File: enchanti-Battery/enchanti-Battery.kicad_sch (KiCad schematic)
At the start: 19 parts, among them U1 BQ25185DLHR, U2 MAX17262REWL+T, U3 USBLC6-2P6

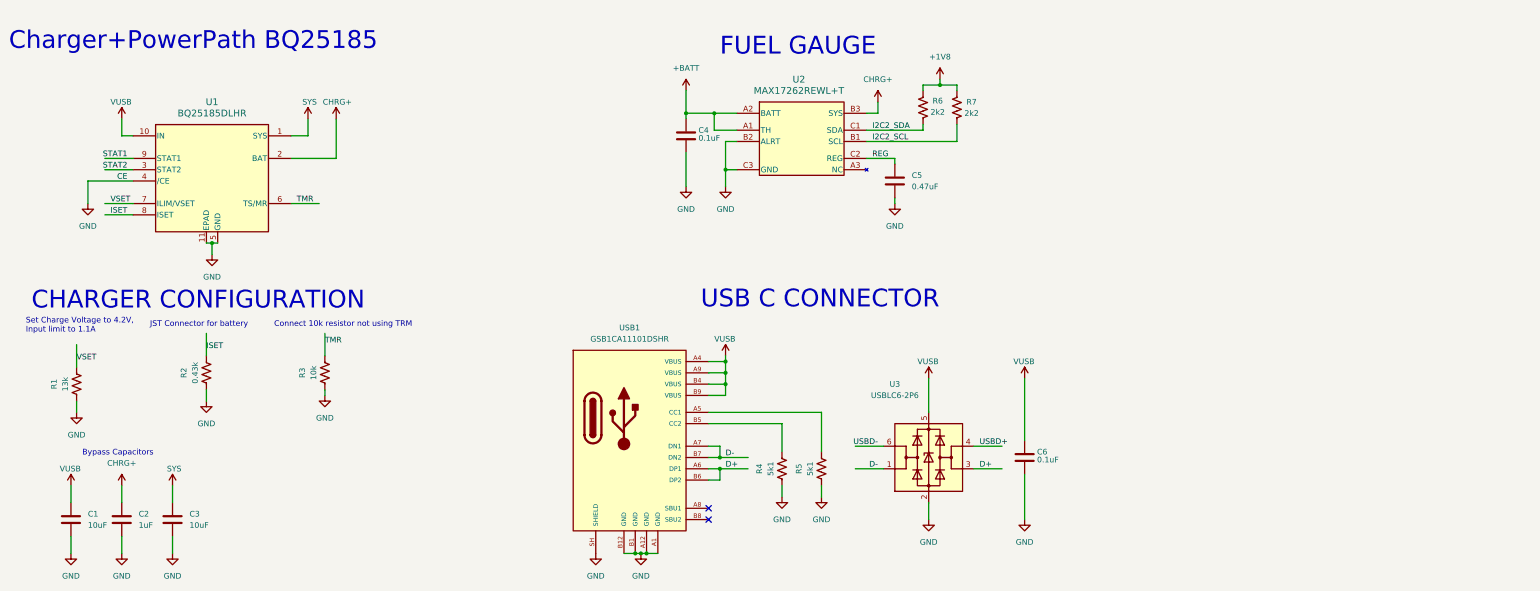
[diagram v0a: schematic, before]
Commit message: added components to 2S battery charger, changing up the enchanti module design
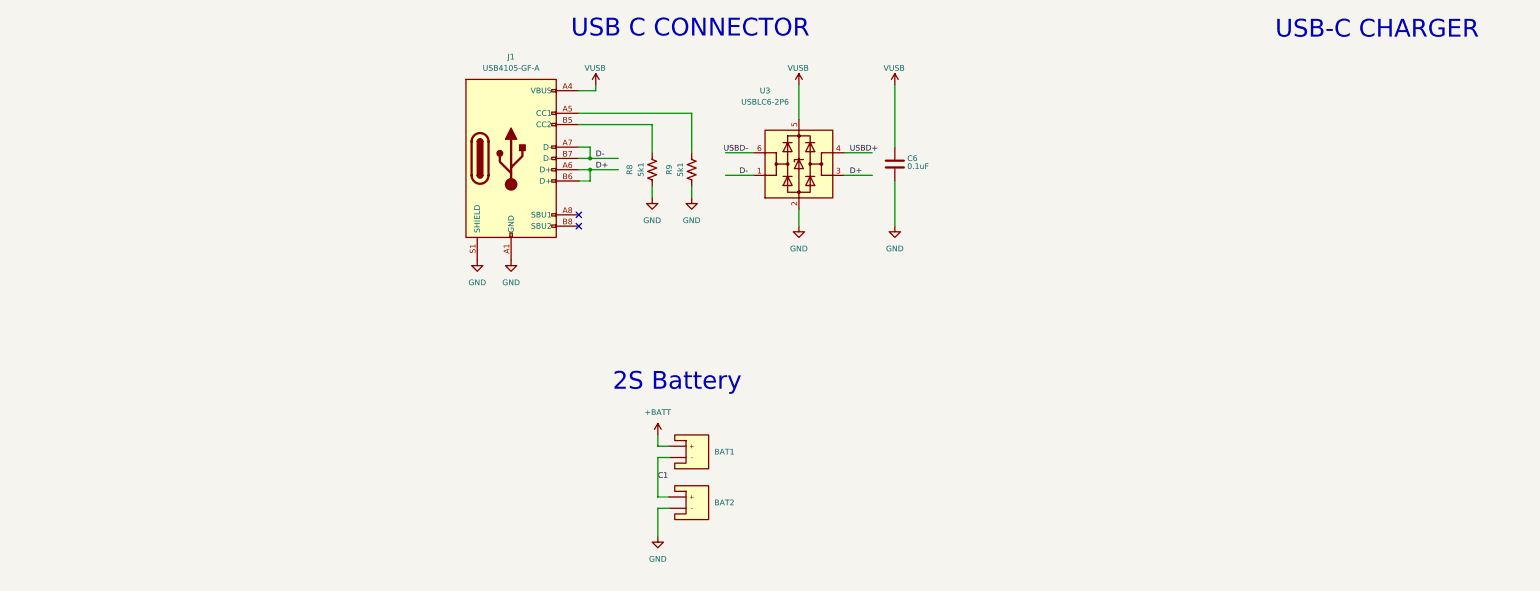
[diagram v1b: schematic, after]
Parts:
- removed C1, C3: 10uF, Capacitor_SMD:C_0603_1608Metric, symbol Device:C
- removed C2: 1uF, Capacitor_SMD:C_0402_1005Metric, symbol Device:C
- removed C4: 0.1uF, Capacitor_SMD:C_0402_1005Metric, symbol Device:C
- removed C5: 0.47uF, Capacitor_SMD:C_0402_1005Metric, symbol Device:C
- removed R1: 13k, Resistor_SMD:R_0402_1005Metric, symbol Device:R_US
- removed R2: 0.43k, Resistor_SMD:R_0402_1005Metric, symbol Device:R_US
- removed R3: 10k, Resistor_SMD:R_0402_1005Metric, symbol Device:R_US
- removed R4, R5: 5k1, Resistor_SMD:R_0402_1005Metric, symbol Device:R_US
- removed R6, R7: 2k2, Resistor_SMD:R_0402_1005Metric, symbol Device:R_US
- removed SYS1, SYS2: SYS, symbol power-symbols:VSYS
- removed U1: BQ25185DLHR, ENCHANTI_battery-management:WSON10_DLH_TEX, symbol ENCHANTI_battery-management:BQ25185DLHR
- removed U2: MAX17262REWL+T, ENCHANTI_battery-management:MAX17262, symbol ENCHANTI_battery-management:MAX17262REWL+T
- removed USB1: GSB1CA11101DSHR, ENCHANTI_connectors:AMPHENOL_GSB1CA11101DSHR, symbol ENCHANTI_connectors:GSB1CA11101DSHR
- added BAT1, BAT2: 18650_HOLDER, Battery:BatteryHolder_MPD_BH-18650-PC2, symbol ENCHANTI_connectors:Battery_18650
- added J1: USB4105-GF-A, Connector_USB:USB_C_Receptacle_GCT_USB4105-xx-A_16P_TopMnt_Horizontal, symbol ENCHANTI_connectors:USB4105-GF-A
- added R8, R9: 5k1, Resistor_SMD:R_0402_1005Metric, symbol Device:R_US
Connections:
- net +BATT: now also BAT1.1 (+)
- net D+: now also J1.A6 (D+), J1.B6 (D+)
- net D-: now also J1.A7 (D-), J1.B7 (D-)
- net GND: now also BAT2.2 (-), J1.A1 (GND), J1.A12 (GND), J1.B1 (GND), J1.B12 (GND), J1.S1 (SHIELD), R8.1, R9.1
- net VUSB: now also J1.A4 (VBUS), J1.A9 (VBUS), J1.B4 (VBUS), J1.B9 (VBUS)
- new net: J1.A5 (CC1), R9.2
- new net: J1.B5 (CC2), R8.2
- new net C1: BAT1.2 (-), BAT2.1 (+)
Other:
- note added: "2S Battery"
- note added: "USB-C CHARGER"
- note removed: "Bypass Capacitors"
- note removed: "CHARGER CONFIGURATION"
- note removed: "Charger+PowerPath BQ25185"
- note removed: "Connect 10k resistor not using TRM"
- note removed: "FUEL GAUGE"
- note removed: "JST Connector for battery"
- note removed: "Set Charge Voltage to 4.2V, Input limit to 1.1A"
- moved on the sheet: C6, U3

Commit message: Revert "added components to 2S battery charger, changing up the enchanti module design"
This reverts commit 22a1e749752c1cc608d102de7de6baf7b482e290.
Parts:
- removed BAT1, BAT2: 18650_HOLDER, Battery:BatteryHolder_MPD_BH-18650-PC2, symbol ENCHANTI_connectors:Battery_18650
- removed J1: USB4105-GF-A, Connector_USB:USB_C_Receptacle_GCT_USB4105-xx-A_16P_TopMnt_Horizontal, symbol ENCHANTI_connectors:USB4105-GF-A
- removed R8, R9: 5k1, Resistor_SMD:R_0402_1005Metric, symbol Device:R_US
- added C1, C3: 10uF, Capacitor_SMD:C_0603_1608Metric, symbol Device:C
- added C2: 1uF, Capacitor_SMD:C_0402_1005Metric, symbol Device:C
- added C4: 0.1uF, Capacitor_SMD:C_0402_1005Metric, symbol Device:C
- added C5: 0.47uF, Capacitor_SMD:C_0402_1005Metric, symbol Device:C
- added R1: 13k, Resistor_SMD:R_0402_1005Metric, symbol Device:R_US
- added R2: 0.43k, Resistor_SMD:R_0402_1005Metric, symbol Device:R_US
- added R3: 10k, Resistor_SMD:R_0402_1005Metric, symbol Device:R_US
- added R4, R5: 5k1, Resistor_SMD:R_0402_1005Metric, symbol Device:R_US
- added R6, R7: 2k2, Resistor_SMD:R_0402_1005Metric, symbol Device:R_US
- added SYS1, SYS2: SYS, symbol power-symbols:VSYS
- added U1: BQ25185DLHR, ENCHANTI_battery-management:WSON10_DLH_TEX, symbol ENCHANTI_battery-management:BQ25185DLHR
- added U2: MAX17262REWL+T, ENCHANTI_battery-management:MAX17262, symbol ENCHANTI_battery-management:MAX17262REWL+T
- added USB1: GSB1CA11101DSHR, ENCHANTI_connectors:AMPHENOL_GSB1CA11101DSHR, symbol ENCHANTI_connectors:GSB1CA11101DSHR
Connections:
- net +BATT: now also C4.1, U2.A1 (TH), U2.A2 (BATT)
- net D+: now also USB1.A6 (DP1), USB1.B6 (DP2)
- net D-: now also USB1.A7 (DN1), USB1.B7 (DN2)
- net GND: now also C1.2, C2.2, C3.2, C4.2, C5.2, R1.1, R2.1, R3.1, R4.1, R5.1, U1.11 (EPAD), U1.4 (/CE), U1.5 (GND), U2.B2 (ALRT), U2.C3 (GND), USB1.A1 (GND), USB1.A12 (GND), USB1.B1 (GND), USB1.B12 (GND), USB1.SH (SHIELD)
- net VUSB: now also C1.1, U1.10 (IN), USB1.A4 (VBUS), USB1.A9 (VBUS), USB1.B4 (VBUS), USB1.B9 (VBUS)
- new net: R5.2, USB1.A5 (CC1)
- new net: R4.2, USB1.B5 (CC2)
- new net +1V8: R6.2, R7.2
- new net CHRG+: C2.1, U1.2 (BAT), U2.B3 (SYS)
- new net I2C2_SCL: R7.1, U2.B1 (SCL)
- new net I2C2_SDA: R6.1, U2.C1 (SDA)
- new net ISET: R2.2, U1.8 (ISET)
- new net REG: C5.1, U2.C2 (REG)
- new net STAT1: U1.9 (STAT1)
- new net STAT2: U1.3 (STAT2)
- new net SYS: C3.1, SYS1.1 (SYS), SYS2.1 (SYS), U1.1 (SYS)
- new net TMR: R3.2, U1.6 (TS/MR)
- new net VSET: R1.2, U1.7 (ILIM/VSET)
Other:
- note added: "Bypass Capacitors"
- note added: "CHARGER CONFIGURATION"
- note added: "Charger+PowerPath BQ25185"
- note added: "Connect 10k resistor not using TRM"
- note added: "FUEL GAUGE"
- note added: "JST Connector for battery"
- note added: "Set Charge Voltage to 4.2V, Input limit to 1.1A"
- note removed: "2S Battery"
- note removed: "USB-C CHARGER"
- moved on the sheet: C6, U3
